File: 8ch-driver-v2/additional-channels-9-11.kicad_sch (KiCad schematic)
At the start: 42 parts, among them Q3 2N7002E, Q4 2N7002E, Q5 2N7002E, U3 DRV104PWP, U4 DRV104PWP, U5 DRV104PWP

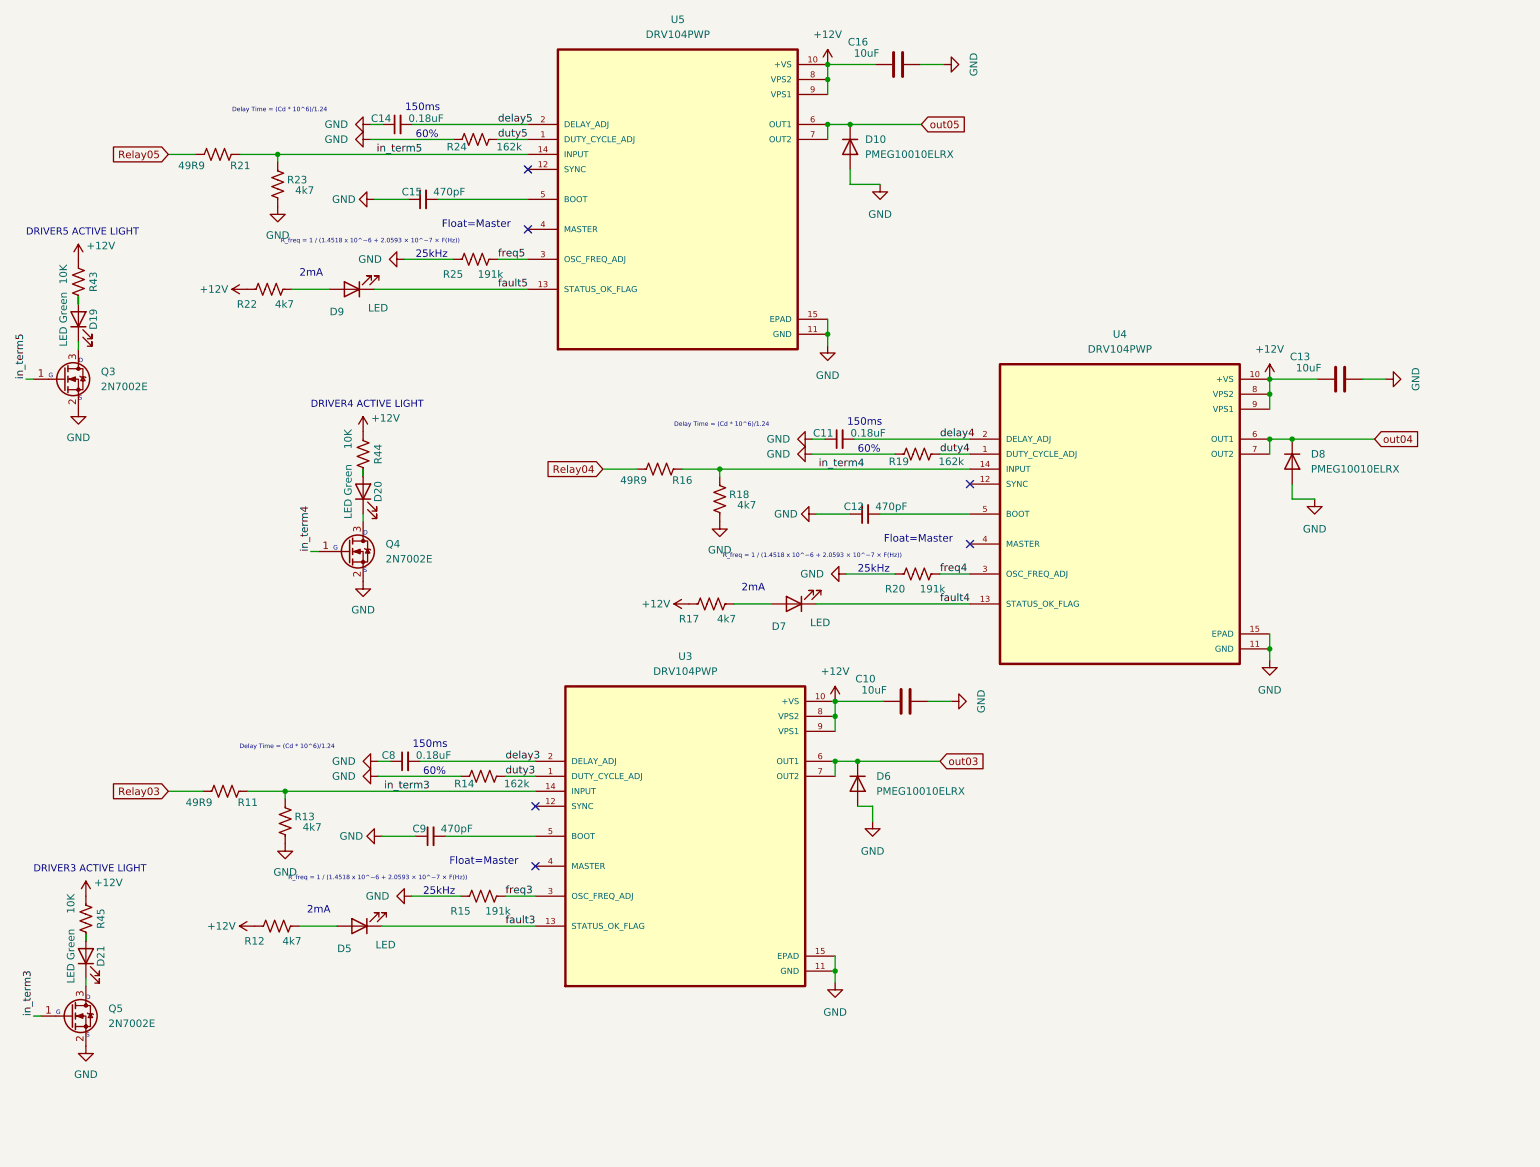
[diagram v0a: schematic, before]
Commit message: added 8 more channels and an FTDH chip
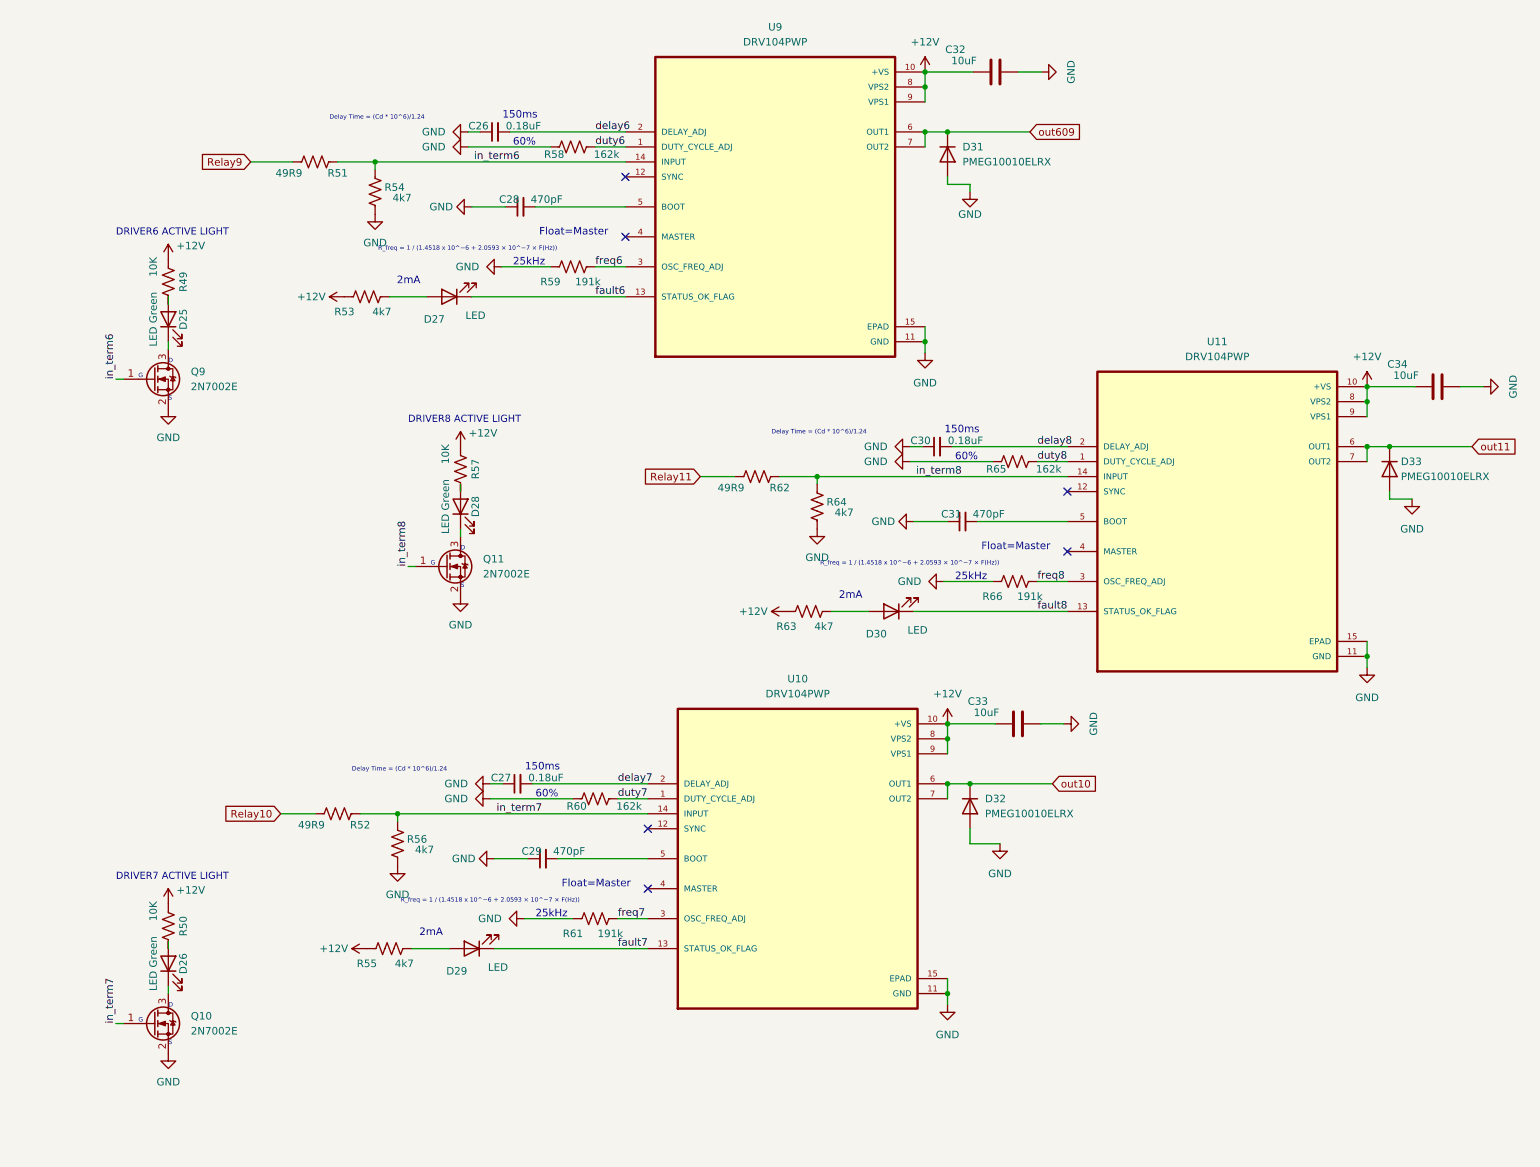
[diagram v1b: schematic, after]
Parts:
- removed C10, C13, C16: 10uF, Capacitor_SMD:C_1210_3225Metric, symbol Device:C
- removed C11, C14, C8: 0.18uF, Capacitor_SMD:C_1206_3216Metric, symbol Device:C_Small
- removed C12, C15, C9: 470pF, Capacitor_SMD:C_1206_3216Metric, symbol Device:C_Small
- removed D10, D6, D8: PMEG10010ELRX, Diode_SMD:Nexperia_CFP3_SOD-123W, symbol Device:D
- removed D19, D20, D21: LED Green, LED_SMD:LED_0805_2012Metric, symbol Device:LED
- removed D5, D7, D9: LED, LED_SMD:LED_0805_2012Metric, symbol Device:LED
- removed Q3, Q4, Q5: 2N7002E, Package_TO_SOT_SMD:SOT-23, symbol Transistor_FET:2N7002E
- removed R11, R16, R21: 49R9, Resistor_SMD:R_1206_3216Metric, symbol Device:R_US
- removed R12, R13, R17, R18, R22, R23: 4k7, Resistor_SMD:R_1206_3216Metric, symbol Device:R_US
- removed R14, R19, R24: 162k, Resistor_SMD:R_1206_3216Metric, symbol Device:R_US
- removed R15, R20, R25: 191k, Resistor_SMD:R_1206_3216Metric, symbol Device:R_US
- removed R43, R44, R45: 10K, Resistor_SMD:R_1206_3216Metric, symbol Device:R_US
- removed U3, U4, U5: DRV104PWP, Solenoid_Driver:IC_TPS27S100BPWPR, symbol DRV104PWP:DRV104PWP
- added C26, C27, C30: 0.18uF, Capacitor_SMD:C_1206_3216Metric, symbol Device:C_Small
- added C28, C29, C31: 470pF, Capacitor_SMD:C_1206_3216Metric, symbol Device:C_Small
- added C32, C33, C34: 10uF, Capacitor_SMD:C_1210_3225Metric, symbol Device:C
- added D25, D26, D28: LED Green, LED_SMD:LED_0805_2012Metric, symbol Device:LED
- added D27, D29, D30: LED, LED_SMD:LED_0805_2012Metric, symbol Device:LED
- added D31, D32, D33: PMEG10010ELRX, Diode_SMD:Nexperia_CFP3_SOD-123W, symbol Device:D
- added Q10, Q11, Q9: 2N7002E, Package_TO_SOT_SMD:SOT-23, symbol Transistor_FET:2N7002E
- added R49, R50, R57: 10K, Resistor_SMD:R_1206_3216Metric, symbol Device:R_US
- added R51, R52, R62: 49R9, Resistor_SMD:R_1206_3216Metric, symbol Device:R_US
- added R53, R54, R55, R56, R63, R64: 4k7, Resistor_SMD:R_1206_3216Metric, symbol Device:R_US
- added R58, R60, R65: 162k, Resistor_SMD:R_1206_3216Metric, symbol Device:R_US
- added R59, R61, R66: 191k, Resistor_SMD:R_1206_3216Metric, symbol Device:R_US
- added U10, U11, U9: DRV104PWP, Solenoid_Driver:IC_TPS27S100BPWPR, symbol DRV104PWP:DRV104PWP
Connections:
- net +12V: now also C32.1, C33.1, C34.1, R49.1, R50.1, R53.1, R55.1, R57.1, R63.1, U10.10 (+VS), U10.8 (VPS2), U10.9 (VPS1), U11.10 (+VS), U11.8 (VPS2), U11.9 (VPS1), U9.10 (+VS), U9.8 (VPS2), U9.9 (VPS1)
- net GND: now also C26.1, C27.1, C28.1, C29.1, C30.1, C31.1, C32.2, C33.2, C34.2, D31.2 (A), D32.2 (A), D33.2 (A), Q10.2 (S), Q11.2 (S), Q9.2 (S), R54.1, R56.1, R58.1, R59.1, R60.1, R61.1, R64.1, R65.1, R66.1, U10.11 (GND), U10.15 (EPAD), U11.11 (GND), U11.15 (EPAD), U9.11 (GND), U9.15 (EPAD)
- new net: D27.2 (A), R53.2
- new net: D26.2 (A), R50.2
- new net: D25.1 (K), Q9.3 (D)
- new net: D25.2 (A), R49.2
- new net: C31.2, U11.5 (BOOT)
- new net: C29.2, U10.5 (BOOT)
- new net: D28.1 (K), Q11.3 (D)
- new net: C28.2, U9.5 (BOOT)
- new net: D30.2 (A), R63.2
- new net: D28.2 (A), R57.2
- new net: D29.2 (A), R55.2
- new net: D26.1 (K), Q10.3 (D)
- new net Relay10: R52.1
- new net Relay11: R62.1
- new net Relay9: R51.1
- new net delay6: C26.2, U9.2 (DELAY_ADJ)
- new net delay7: C27.2, U10.2 (DELAY_ADJ)
- new net delay8: C30.2, U11.2 (DELAY_ADJ)
- new net duty6: R58.2, U9.1 (DUTY_CYCLE_ADJ)
- new net duty7: R60.2, U10.1 (DUTY_CYCLE_ADJ)
- new net duty8: R65.2, U11.1 (DUTY_CYCLE_ADJ)
- new net fault6: D27.1 (K), U9.13 (STATUS_OK_FLAG)
- new net fault7: D29.1 (K), U10.13 (STATUS_OK_FLAG)
- new net fault8: D30.1 (K), U11.13 (STATUS_OK_FLAG)
- new net freq6: R59.2, U9.3 (OSC_FREQ_ADJ)
- new net freq7: R61.2, U10.3 (OSC_FREQ_ADJ)
- new net freq8: R66.2, U11.3 (OSC_FREQ_ADJ)
- new net in_term6: Q9.1 (G), R51.2, R54.2, U9.14 (INPUT)
- new net in_term7: Q10.1 (G), R52.2, R56.2, U10.14 (INPUT)
- new net in_term8: Q11.1 (G), R62.2, R64.2, U11.14 (INPUT)
- new net out10: D32.1 (K), U10.6 (OUT1), U10.7 (OUT2)
- new net out11: D33.1 (K), U11.6 (OUT1), U11.7 (OUT2)
- new net out609: D31.1 (K), U9.6 (OUT1), U9.7 (OUT2)
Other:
- note added: "DRIVER6 ACTIVE LIGHT"
- note added: "DRIVER7 ACTIVE LIGHT"
- note added: "DRIVER8 ACTIVE LIGHT"
- note removed: "DRIVER3 ACTIVE LIGHT"
- note removed: "DRIVER4 ACTIVE LIGHT"
- note removed: "DRIVER5 ACTIVE LIGHT"
- company: Boston University -> (none)

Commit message: progress
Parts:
- U9: footprint Solenoid_Driver:IC_TPS27S100BPWPR -> Solenoid_Driver:PWP14_2P31X2P46
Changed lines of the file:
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@@
 			)
 		)
-		(property "Footprint" "Solenoid_Driver:IC_TPS27S100BPWPR"
+		(property "Footprint" "Solenoid_Driver:PWP14_2P31X2P46"
 			(at 147.32 45.72 0)
 			(effects

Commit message: mucho mas progresso
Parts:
- removed C26: 0.18uF, Capacitor_SMD:C_1206_3216Metric, symbol Device:C_Small
- removed C29: 470pF, Capacitor_SMD:C_1206_3216Metric, symbol Device:C_Small
- removed C33, C34: 10uF, Capacitor_SMD:C_1210_3225Metric, symbol Device:C
- removed D25, D28: LED Green, LED_SMD:LED_0805_2012Metric, symbol Device:LED
- removed D32, D33: PMEG10010ELRX, Diode_SMD:Nexperia_CFP3_SOD-123W, symbol Device:D
- added C26, C29: 10uF, Capacitor_SMD:C_1210_3225Metric, symbol Device:C
- added C33: 0.18uF, Capacitor_SMD:C_1206_3216Metric, symbol Device:C_Small
- added C34: 470pF, Capacitor_SMD:C_1206_3216Metric, symbol Device:C_Small
- added D25, D28: PMEG10010ELRX, Diode_SMD:Nexperia_CFP3_SOD-123W, symbol Device:D
- added D32: LED Green, LED_SMD:LED_0805_2012Metric, symbol Device:LED
- added D33: LED, LED_SMD:LED_0805_2012Metric, symbol Device:LED
- D29: value LED -> LED Green
- R50: value 10K -> 162k
- R52: value 49R9 -> 4k7; PartNum RC0805FR-0749R9L -> RC0805JR-074K7L
- R53: value 4k7 -> 191k; PartNum RC0805JR-074K7L -> RC0805FR-07191KL
- R55: value 4k7 -> 10K; PartNum RC0805JR-074K7L -> RC0805FR-07162KL
- R56: value 4k7 -> 162k; PartNum RC0805JR-074K7L -> RC0805FR-07162KL
- R57: value 10K -> 49R9; PartNum RC0805FR-07162KL -> RC0805FR-0749R9L
- R58, R60: value 162k -> 4k7; PartNum RC0805FR-07162KL -> RC0805JR-074K7L
- R61: value 191k -> 10K; PartNum RC0805FR-07191KL -> RC0805FR-07162KL
- R62: value 49R9 -> 162k; PartNum RC0805FR-0749R9L -> RC0805FR-07162KL
- R63: value 4k7 -> 49R9; PartNum RC0805JR-074K7L -> RC0805FR-0749R9L
- R65: value 162k -> 191k; PartNum RC0805FR-07162KL -> RC0805FR-07191KL
- R66: value 191k -> 4k7; PartNum RC0805FR-07191KL -> RC0805JR-074K7L
- U9: footprint Solenoid_Driver:PWP14_2P31X2P46 -> Solenoid_Driver:IC_TPS27S100BPWPR
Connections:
- net +12V: now also R54.1, R60.1, R61.1, R66.1, C26.1, C29.1; no longer R50.1, R53.1, R57.1, R63.1
- net GND: now also R50.1, R52.1, R53.1, R62.1, C26.2, C29.2, C33.1, C34.1, D25.2 (A), D28.2 (A); no longer R54.1, R60.1, R61.1, R66.1
- net Relay10: now also R57.1; no longer R52.1
- net Relay11: now also R63.1; no longer R62.1
- net out10: now also D28.1 (K)
- net out11: now also D31.1 (K)
- net at D27.2 (A): now also R54.2; no longer R53.2
- net at D26.2 (A): now also R49.2; no longer R50.2
- net at Q9.3 (D): now also D26.1 (K)
- net at C31.2: now also U10.5 (BOOT); no longer U11.5 (BOOT)
- net at Q11.3 (D): now also D32.1 (K)
- net at D30.2 (A): now also R60.2; no longer R63.2
- net in_term10: now reaches R57.2
- net in_term10: now also Q10.1 (G), R58.2, U10.14 (INPUT)
- net at Q10.3 (D): now also D29.1 (K); no longer D26.1 (K)
- net Relay9 renamed Relay09
- net delay6 renamed delay09
- net delay09: now also C27.2
- net delay7 renamed delay10
- net delay10: now also C30.2; no longer C27.2
- net delay8 renamed delay11
- net delay11: now also C33.2; no longer C30.2
- net duty6 renamed duty09
- net duty09: now also R50.2; no longer R58.2
- net duty7 renamed duty10
- net duty10: now also R56.2; no longer R60.2
- net duty8 renamed duty11
- net duty11: now also R62.2; no longer R65.2
- net fault6 renamed fault09
- net fault7 renamed fault10
- net fault10: now also D30.1 (K); no longer D29.1 (K)
- net fault8 renamed fault11
- net fault11: now also D33.1 (K); no longer D30.1 (K)
- net freq6 renamed freq09
- net freq09: now also R53.2; no longer R59.2
- net freq7: no longer names the net of R61.2
- net freq7: now also D32.2 (A); no longer U10.3 (OSC_FREQ_ADJ)
- net freq8: no longer names the net of R66.2
- net freq8: now also D33.2 (A); no longer U11.3 (OSC_FREQ_ADJ)
- net in_term6 renamed in_term09
- net in_term09: now also R52.2; no longer R54.2
- removed net in_term7: Q10.1 (G), R52.2, R56.2, U10.14 (INPUT)
- net in_term8 renamed in_term11
- net in_term11: now also R63.2; no longer R62.2
- net out609 renamed out09
- net out09: now also D25.1 (K); no longer D31.1 (K)
- new net: C34.2, U11.5 (BOOT)
- new net freq10: R59.2, U10.3 (OSC_FREQ_ADJ)
- new net freq11: R65.2, U11.3 (OSC_FREQ_ADJ)
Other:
- note removed: "DRIVER7 ACTIVE LIGHT"
- note removed: "DRIVER8 ACTIVE LIGHT"
